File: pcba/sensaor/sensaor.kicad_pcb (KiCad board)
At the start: 2 copper layers, 18 parts, among them J1 SAO, J12 Conn_01x09_Pin, J13 Conn_01x09_Pin, J2 WS2812, J3 Conn_01x09_Pin, J4 Conn_01x09_Pin, J5 Conn_01x09_Pin, J6 Programming, J7 Speed, J8 Shape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

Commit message: Update PCB
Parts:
- removed J12, J13: Conn_01x09_Pin, Connector_PinHeader_2.54mm:PinHeader_1x09_P2.54mm_Vertical
- J1: moved to B.Cu
- J2: footprint Connector_Harwin:Harwin_M20-89003xx_1x03_P2.54mm_Horizontal -> Connector_PinHeader_2.54mm:PinHeader_1x03_P2.54mm_Vertical
- J3, J4, J5: value Conn_01x09_Pin -> Conn_01x10_Pin; footprint Connector_PinHeader_2.54mm:PinHeader_1x09_P2.54mm_Vertical -> Connector_PinHeader_2.54mm:PinHeader_1x10_P2.54mm_Vertical
- J7: value Speed -> Conn_01x10_Pin; footprint Connector_PinHeader_2.54mm:PinHeader_1x03_P2.54mm_Vertical -> Connector_PinHeader_2.54mm:PinHeader_1x10_P2.54mm_Vertical
- J8: value Shape -> Conn_01x10_Pin; footprint Connector_PinHeader_2.54mm:PinHeader_1x03_P2.54mm_Vertical -> Connector_PinHeader_2.54mm:PinHeader_1x10_P2.54mm_Vertical
- J9: value CONF -> Conn_01x10_Pin; footprint Connector_PinHeader_2.54mm:PinHeader_1x03_P2.54mm_Vertical -> Connector_PinHeader_2.54mm:PinHeader_1x10_P2.54mm_Vertical
- R1, R2: footprint Resistor_SMD:R_0201_0603Metric_Pad0.64x0.40mm_HandSolder -> Capacitor_SMD:C_0402_1005Metric_Pad0.74x0.62mm_HandSolder
- moved D1 36.7 mm to (79.0, 79.5), turned to -90 degrees
- moved J7 22.6 mm to (107.3, 72.0), turned to 90 degrees
- moved D2 22.5 mm to (79.0, 69.4), turned to -90 degrees
- moved J6 19.8 mm to (87.0, 78.5), turned to 90 degrees
- moved R1 15.5 mm to (96.0, 78.0), turned to -90 degrees
- moved J1 15.2 mm to (92.5, 59.0), turned to -90 degrees
- moved J9 14.4 mm to (107.3, 80.0), turned to 90 degrees
- moved J5 10.2 mm to (107.4, 68.0), turned to 90 degrees
- moved R2 9.12 mm to (98.5, 78.0), turned to -90 degrees
- moved J8 8.57 mm to (107.3, 76.0), turned to 90 degrees
- moved D3 7.14 mm to (79.0, 58.5), turned to -90 degrees
- moved J2 6.12 mm to (76.0, 51.5), turned to 90 degrees
- moved J4 4.56 mm to (107.3, 64.0), turned to 90 degrees
- moved J3 1.37 mm to (107.3, 60.0), turned to 90 degrees
- moved C1 0.62 mm to (97.5, 66.0)
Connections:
- net /LED0 renamed /LED
- J3 pad 1: VCC -> /SPEED
- J3 pad 3: /AR -> unconnected-(J3-Pin_3-Pad3)
- J3 pad 5: /AG -> unconnected-(J3-Pin_5-Pad5)
- J3 pad 7: /AB -> unconnected-(J3-Pin_7-Pad7)
- J3 pad 9: GND -> unconnected-(J3-Pin_9-Pad9)
- J4 pad 1: VCC -> /SHAPE
- J4 pad 9: GND -> unconnected-(J4-Pin_9-Pad9)
- J5 pad 1: VCC -> /PHASE
- J5 pad 9: GND -> unconnected-(J5-Pin_9-Pad9)
- J7 pad 1: VCC -> /AR
- J7 pad 2: /SPEED -> unconnected-(J7-Pin_2-Pad2)
- J7 pad 3: GND -> unconnected-(J7-Pin_3-Pad3)
- J8 pad 1: VCC -> /AG
- J8 pad 2: /SHAPE -> unconnected-(J8-Pin_2-Pad2)
- J8 pad 3: GND -> unconnected-(J8-Pin_3-Pad3)
- J9 pad 1: VCC -> /AB
- J9 pad 2: /CONF -> unconnected-(J9-Pin_2-Pad2)
- J9 pad 3: GND -> unconnected-(J9-Pin_3-Pad3)
- U1 pad 12: /SHAPE -> /PHASE
- U1 pad 13: /CONF -> /SHAPE
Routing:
- net GND: track 116.3 -> 147.7 mm, vias 1 -> 2
- net /CONF: track 21.5 -> 0.00 mm, vias 2 -> 0
- net /LED: track 31.1 -> 16.7 mm
- net /PHASE: track 0.00 -> 13.9 mm
- net /ID0: track 2.83 -> 15.1 mm, vias 0 -> 2
- net /ID1: track 3.27 -> 10.9 mm, vias 0 -> 2
- net /SPEED: track 17.2 -> 23.2 mm, vias 2 -> 0
- net /GPIO2: track 8.50 -> 14.4 mm, vias 0 -> 1
- net /SWIO: track 13.8 -> 8.84 mm, vias 2 -> 1
- net /AR: track 17.6 -> 13.8 mm
- net /AG: track 18.9 -> 15.7 mm, vias 0 -> 1
- net /AB: track 17.9 -> 21.1 mm
- net /SDA: track 11.8 -> 9.16 mm
- net /SHAPE: track 17.2 -> 15.0 mm, vias 1 -> 0
- net VCC: track 130.2 -> 128.4 mm, vias 0 -> 2
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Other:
- board outline added: 63.5 x 39 mm
- board text added: "3.3V"
- board text added: "Blue"
- board text added: "DIN"
- board text added: "GND"
- board text added: "GPIO1"
- board text added: "GPIO2"
- board text added: "Green"
- board text added: "Phase"
- board text added: "Programming"
- board text added: "Red"
- board text added: "SCL"
- board text added: "SDA"
- board text added: "SWIO"
- board text added: "Shape"
- board text added: "Speed"
- board text added: "https://github.com/bwasserm/sensaor"
- board text added: "senSAOr"
- board text added: "v0.9"

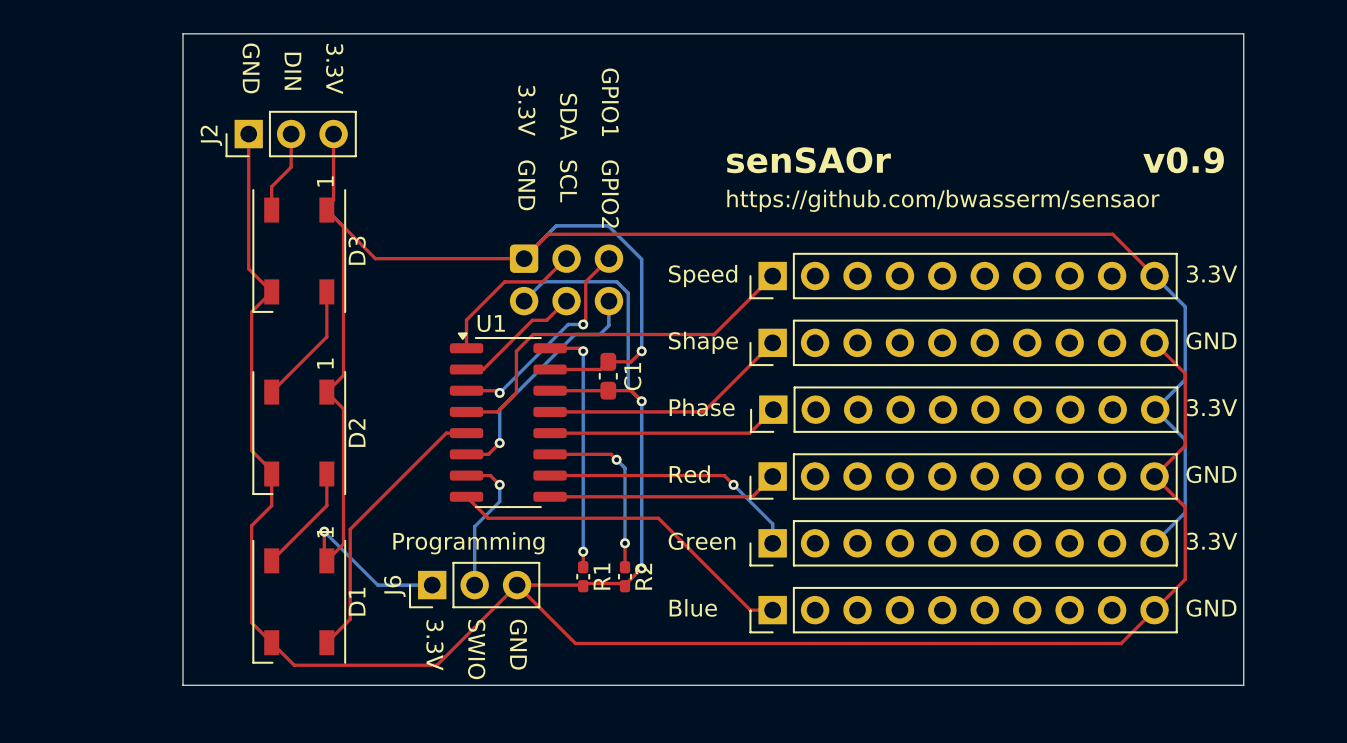
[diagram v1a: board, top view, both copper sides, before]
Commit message: Shrink board and fix DRC
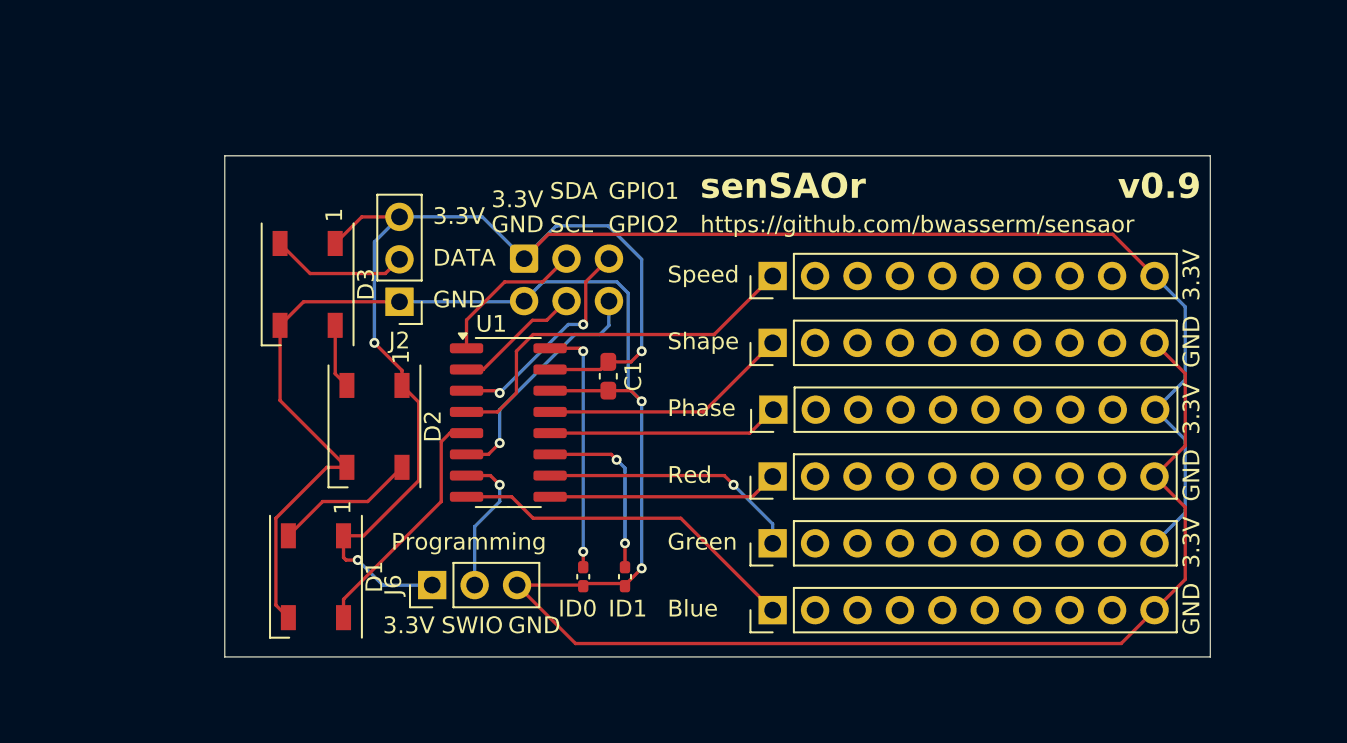
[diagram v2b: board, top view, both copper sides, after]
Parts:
- moved J2 13.5 mm to (85.0, 61.5), turned to 180 degrees
- moved D2 4.52 mm to (83.5, 69.0)
- moved D3 2.06 mm to (79.5, 60.5)
- moved D1 1.80 mm to (80.0, 78.0)
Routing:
- net GND: track 147.7 -> 134.8 mm
- net VCC: track 128.4 -> 122.3 mm, vias 2 -> 3
- net Net-(D2-DOUT): track 7.37 -> 3.89 mm
- net Net-(D3-DOUT): track 5.03 -> 8.25 mm
- net /LED: track 16.7 -> 14.7 mm
- net Net-(D1-DOUT): track 6.57 -> 8.50 mm
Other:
- board size 63.5 x 39 mm -> 59 x 30 mm
- board text added: "DATA"
- board text added: "ID0"
- board text added: "ID1"
- board text removed: "DIN"

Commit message: Add ground pours, update silkscreen
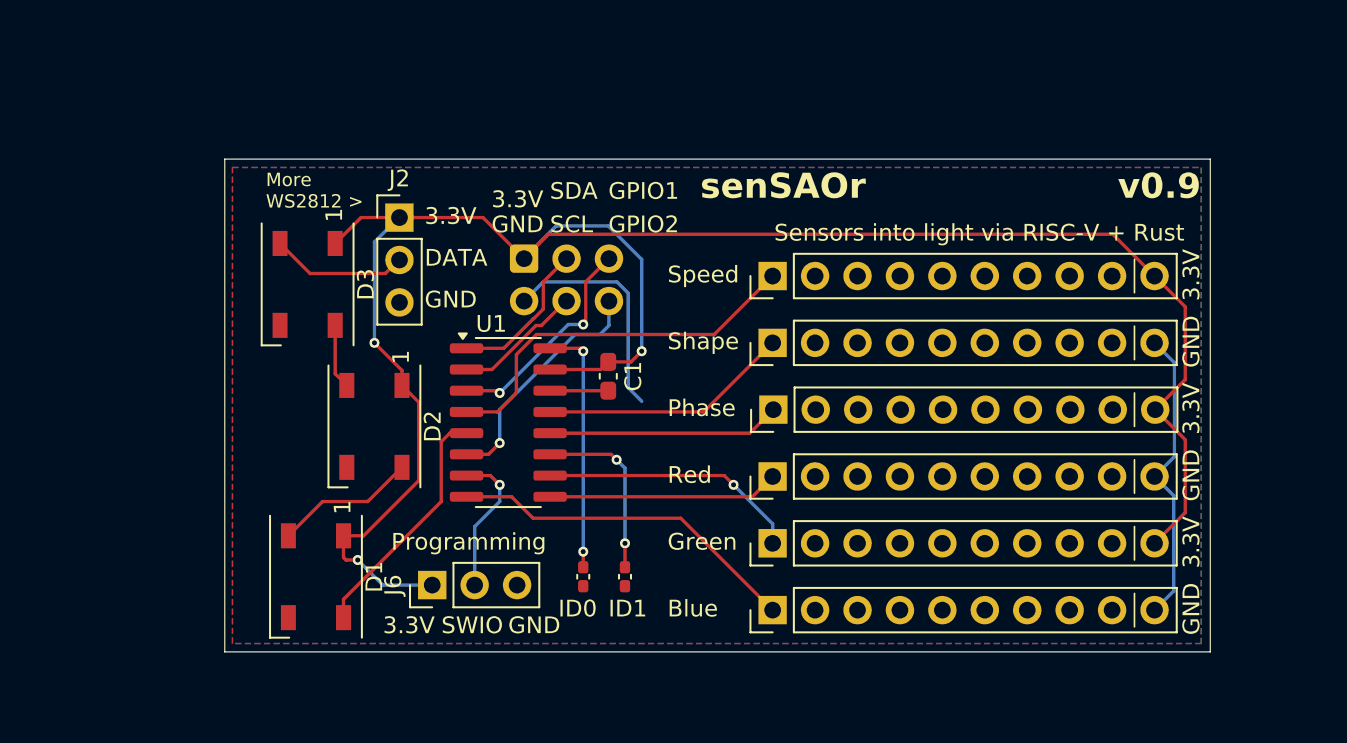
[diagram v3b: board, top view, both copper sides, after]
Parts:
- moved J2 5.04 mm to (85.0, 56.5), turned to 0 degrees
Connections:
- J2 pad 1: GND -> VCC
- J2 pad 3: VCC -> GND
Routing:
- net GND: track 134.8 -> 36.3 mm, vias 2 -> 0
- added copper zone on B.Cu, net GND
- added copper zone on F.Cu, net GND
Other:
- board size 59 x 30 mm -> 59 x 29.5 mm
- board text added: "0-3.3: Control input range RGB: Pulse intensity dim-bright Speed: Pulse update rate slow-fast Shape: Narrow to wide (always on) Phase: inter-color 0-60deg delays"
- board text added: "More WS2812 >"
- board text added: "Sensors into light via RISC-V + Rust"

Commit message: Moving some traces
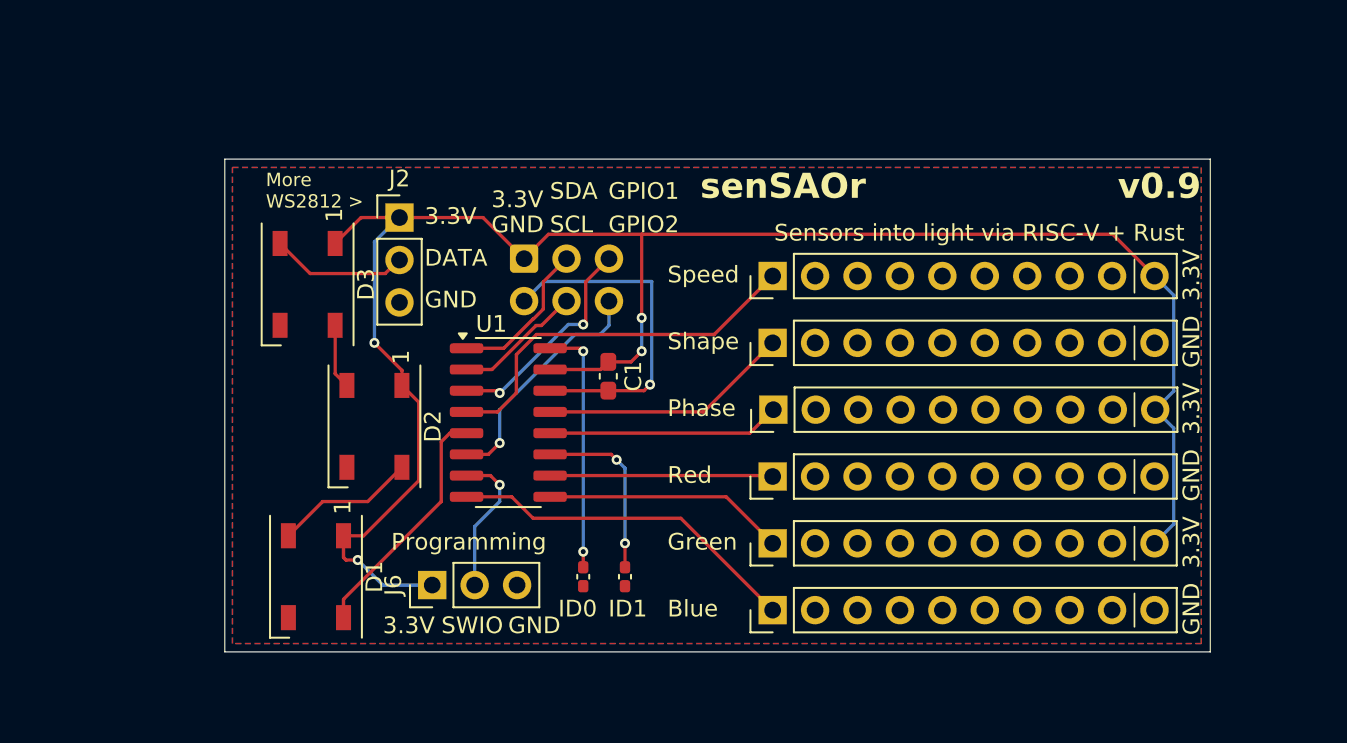
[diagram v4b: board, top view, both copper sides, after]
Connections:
- U1 pad 10: /AG -> /AR
- U1 pad 9: /AR -> /AG
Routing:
- net GND: track 36.3 -> 21.5 mm, vias 0 -> 1
- net VCC: track 122.3 -> 113.9 mm, vias 3 -> 4
- net /AG: track 15.7 -> 14.5 mm, vias 1 -> 0
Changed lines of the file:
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@@
 			(layers "F.Cu" "F.Paste" "F.Mask")
 			(roundrect_rratio 0.25)
-			(net 11 "/AR")
+			(net 12 "/AG")
 			(pinfunction "PD5")
 			(pintype "bidirectional")
@@
 			(layers "F.Cu" "F.Paste" "F.Mask")
 			(roundrect_rratio 0.25)
-			(net 12 "/AG")
+			(net 11 "/AR")
 			(pinfunction "PD6")
 			(pintype "bidirectional")
@@
 	)
 	(gr_text "Shape"
-		(at 106 64.5 -0)
+		(at 106 62.5 90)
 		(layer "B.SilkS")
 		(effects
@@
 	)
 	(gr_text "Speed"
-		(at 106 60.5 -0)
+		(at 106 58 90)
 		(layer "B.SilkS")
 		(effects
@@
 	)
 	(segment
-		(start 132.04 69.8)
-		(end 132.04 74.16)
-		(width 0.2)
-		(layer "F.Cu")
-		(net 1)
-	)
-	(segment
-		(start 127.7 57.5)
-		(end 93.92 57.5)
-		(width 0.2)
-		(layer "F.Cu")
-		(net 1)
-	)
-	(segment
-		(start 132.04 66.2)
-		(end 130.24 68)
-		(width 0.2)
-		(layer "F.Cu")
-		(net 1)
-	)
-	(segment
 		(start 82.5 77)
 		(end 81.8 77)
@@
 	)
 	(segment
+		(start 99.5 57.5)
+		(end 93.92 57.5)
+		(width 0.2)
+		(layer "F.Cu")
+		(net 1)
+	)
+	(segment
 		(start 97.5 65.1375)
 		(end 98.8625 65.1375)
@@
 	)
 	(segment
-		(start 132.04 61.84)
-		(end 132.04 66.2)
-		(width 0.2)
-		(layer "F.Cu")
-		(net 1)
-	)
-	(segment
 		(start 92.46 58.96)
 		(end 90 56.5)
@@
 	)
 	(segment
-		(start 132.04 74.16)
-		(end 130.2 76)
-		(width 0.2)
-		(layer "F.Cu")
-		(net 1)
-	)
-	(segment
 		(start 90 56.5)
 		(end 85 56.5)
@@
 	)
 	(segment
+		(start 127.7 57.5)
+		(end 99.5 57.5)
+		(width 0.2)
+		(layer "F.Cu")
+		(net 1)
+	)
+	(segment
 		(start 86.15 72.25)
 		(end 86.15 67.55)
@@
 	)
 	(segment
-		(start 130.2 60)
-		(end 132.04 61.84)
-		(width 0.2)
-		(layer "F.Cu")
-		(net 1)
-	)
-	(segment
 		(start 81.8 77)
 		(end 81.65 76.85)
@@
 	)
 	(segment
-		(start 130.24 68)
-		(end 132.04 69.8)
+		(start 99.5 62.5)
+		(end 99.5 57.5)
 		(width 0.2)
 		(layer "F.Cu")
@@
 		(width 0.2)
 		(layer "F.Cu")
+		(net 1)
+	)
+	(via
+		(at 99.5 62.5)
+		(size 0.6)
+		(drill 0.3)
+		(layers "F.Cu" "B.Cu")
 		(net 1)
 	)
@@
 	)
 	(segment
+		(start 130.2 60)
+		(end 131.35 61.15)
+		(width 0.2)
+		(layer "B.Cu")
+		(net 1)
+	)
+	(segment
+		(start 131.35 61.15)
+		(end 131.35 66.89)
+		(width 0.2)
+		(layer "B.Cu")
+		(net 1)
+	)
+	(segment
 		(start 99.5 64.5)
-		(end 99.5 59)
+		(end 99.5 62.5)
+		(width 0.2)
+		(layer "B.Cu")
+		(net 1)
+	)
+	(segment
+		(start 130.24 68)
+		(end 131.35 69.11)
 		(width 0.2)
 		(layer "B.Cu")
@@
 	)
 	(segment
-		(start 97.5 57)
-		(end 94.38 57)
-		(width 0.2)
-		(layer "B.Cu")
-		(net 1)
-	)
-	(segment
 		(start 83.5 64)
 		(end 83.5 57.96)
@@
 	)
 	(segment
+		(start 131.35 74.85)
+		(end 130.2 76)
+		(width 0.2)
+		(layer "B.Cu")
+		(net 1)
+	)
+	(segment
 		(start 84 78.5)
 		(end 86.96 78.5)
@@
 	)
 	(segment
-		(start 94.38 57)
-		(end 92.42 58.96)
+		(start 131.35 66.89)
+		(end 130.24 68)
 		(width 0.2)
 		(layer "B.Cu")
@@
 	)
 	(segment
-		(start 99.5 59)
-		(end 97.5 57)
+		(start 131.35 69.11)
+		(end 131.35 74.85)
 		(width 0.2)
 		(layer "B.Cu")
@@
 	)
 	(segment
+		(start 99.6375 66.8625)
+		(end 100 66.5)
+		(width 0.2)
+		(layer "F.Cu")
+		(net 2)
+	)
+	(segment
+		(start 97.5 66.8625)
+		(end 99.6375 66.8625)
+		(width 0.2)
+		(layer "F.Cu")
+		(net 2)
+	)
+	(segment
 		(start 92.544314 62)
 		(end 93 62)
@@
 		(net 2)
 	)
-	(segment
-		(start 92.46 61.5)
-		(end 93.61 60.35)
+	(via
+		(at 100 66.5)
+		(size 0.6)
+		(drill 0.3)
+		(layers "F.Cu" "B.Cu")
+		(net 2)
+	)
+	(segment
+		(start 93.633654 60.326346)
+		(end 92.46 61.5)
 		(width 0.2)
 		(layer "B.Cu")
@@
 	)
 	(segment
-		(start 131.35 73.15)
-		(end 131.35 78.85)
+		(start 92.42 61.54)
+		(end 92.46 61.5)
 		(width 0.2)
 		(layer "B.Cu")
@@
 	)
 	(segment
-		(start 130.2 72)
-		(end 131.35 73.15)
+		(start 100.1 60.326346)
+		(end 93.633654 60.326346)
 		(width 0.2)
 		(layer "B.Cu")
@@
 	)
 	(segment
-		(start 130.2 64)
-		(end 131.39 65.19)
+		(start 100.1 66.4)
+		(end 100.1 60.326346)
 		(width 0.2)
 		(layer "B.Cu")
@@
 	)
 	(segment
-		(start 98.69 66.69)
-		(end 99.5 67.5)
-		(width 0.2)
-		(layer "B.Cu")
-		(net 2)
-	)
-	(segment
-		(start 92.42 61.54)
-		(end 92.46 61.5)
-		(width 0.2)
-		(layer "B.Cu")
-		(net 2)
-	)
-	(segment
-		(start 93.61 60.35)
-		(end 98.016346 60.35)
-		(width 0.2)
-		(layer "B.Cu")
-		(net 2)
-	)
-	(segment
-		(start 131.39 65.19)
-		(end 131.39 70.81)
-		(width 0.2)
-		(layer "B.Cu")
-		(net 2)
-	)
-	(segment
-		(start 131.39 70.81)
-		(end 130.2 72)
-		(width 0.2)
-		(layer "B.Cu")
-		(net 2)
-	)
-	(segment
-		(start 131.35 78.85)
-		(end 130.2 80)
-		(width 0.2)
-		(layer "B.Cu")
-		(net 2)
-	)
-	(segment
-		(start 98.69 61.023654)
-		(end 98.69 66.69)
-		(width 0.2)
-		(layer "B.Cu")
-		(net 2)
-	)
-	(segment
-		(start 98.016346 60.35)
-		(end 98.69 61.023654)
+		(start 100 66.5)
+		(end 100.1 66.4)
 		(width 0.2)
 		(layer "B.Cu")
@@
 	)
 	(segment
+		(start 107.285 71.945)
+		(end 107.34 72)
+		(width 0.2)
+		(layer "F.Cu")
+		(net 11)
+	)
+	(segment
+		(start 94.015 71.945)
+		(end 107.285 71.945)
+		(width 0.2)
+		(layer "F.Cu")
+		(net 11)
+	)
+	(segment
 		(start 94.015 73.215)
-		(end 106.125 73.215)
-		(width 0.2)
-		(layer "F.Cu")
-		(net 11)
-	)
-	(segment
-		(start 106.125 73.215)
-		(end 107.34 72)
-		(width 0.2)
-		(layer "F.Cu")
-		(net 11)
-	)
-	(segment
-		(start 94.015 71.945)
-		(end 104.445 71.945)
+		(end 104.555 73.215)
 		(width 0.2)
 		(layer "F.Cu")
@@
 	)
 	(segment
-		(start 104.445 71.945)
-		(end 105 72.5)
+		(start 104.555 73.215)
+		(end 107.34 76)
 		(width 0.2)
 		(layer "F.Cu")
 		(net 12)
 	)
-	(via
-		(at 105 72.5)
-		(size 0.6)
-		(drill 0.3)
-		(layers "F.Cu" "B.Cu")
-		(net 12)
-	)
-	(segment
-		(start 105 72.5)
-		(end 107.34 74.84)
-		(width 0.2)
-		(layer "B.Cu")
-		(net 12)
-	)
-	(segment
-		(start 107.34 74.84)
-		(end 107.34 76)
-		(width 0.2)
-		(layer "B.Cu")
-		(net 12)
-	)

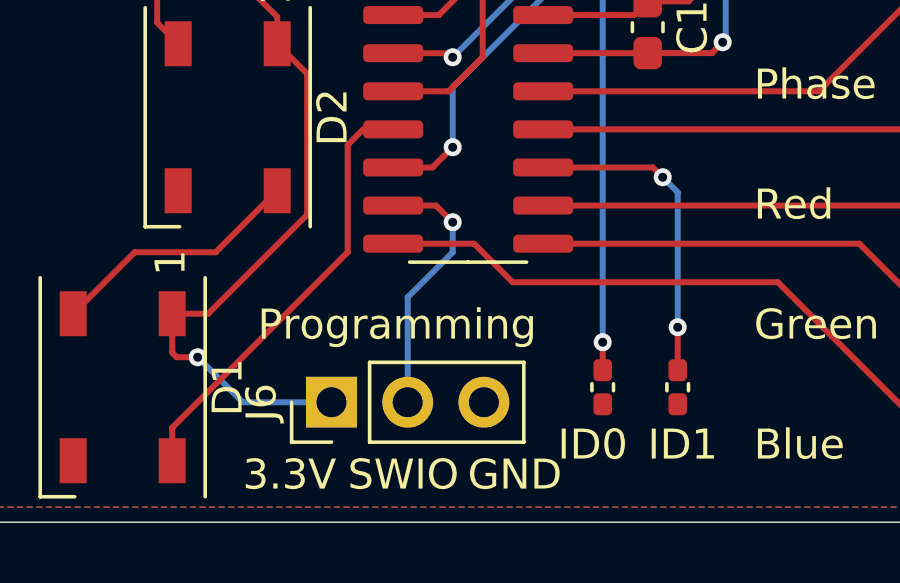
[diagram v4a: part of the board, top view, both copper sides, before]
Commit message: Moved a dimension
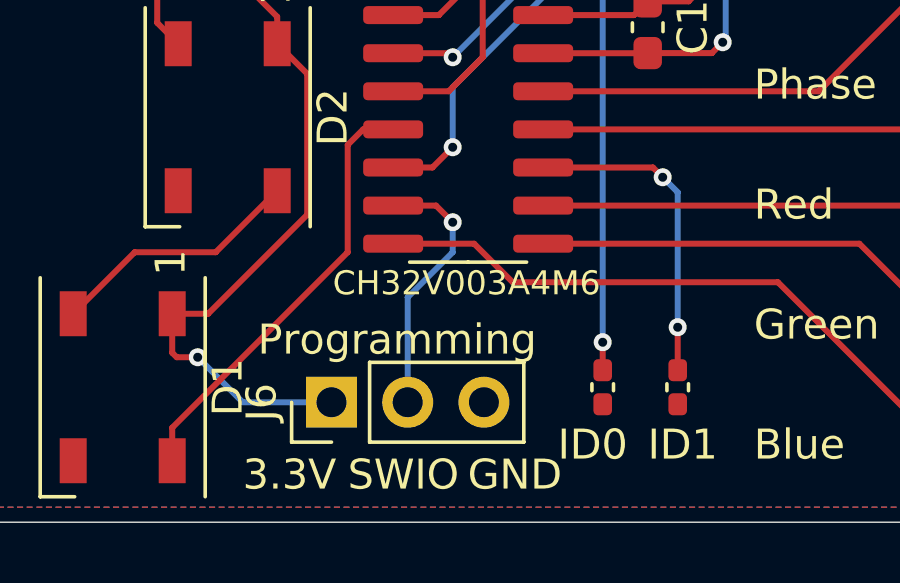
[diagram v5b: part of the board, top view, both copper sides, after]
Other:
- board text added: "CH32V003A4M6"
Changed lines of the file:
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@@
+		)
+	)
+	(gr_text "CH32V003A4M6"
+		(at 87 75 0)
+		(layer "F.SilkS")
+		(effects
+			(font
+				(size 0.8 0.8)
+				(thickness 0.1)
+			)
+			(justify left bottom)
 		)
 	)
@@
 	)
 	(gr_text "Programming"
-		(at 84.5 76.5 0)
+		(at 84.5 77 0)
 		(layer "F.SilkS")
 		(effects
@@
 		)
 		(height 4)
-		(gr_text "59.0000 mm"
+		(gr_text "2322.8346 mils"
 			(at 104.04 85.0025 0)
 			(layer "Cmts.User")
@@
 		(layer "Cmts.User")
 		(pts
-			(xy 133.54 82.8025) (xy 133.54 52.8025)
+			(xy 133.54 82.8025) (xy 133.54 53)
 		)
 		(height 3.46)
-		(gr_text "30.0000 mm"
-			(at 135.2 67.8025 90)
+		(gr_text "1173.3268 mils"
+			(at 135.2 67.90125 90)
 			(layer "Cmts.User")
 			(effects
